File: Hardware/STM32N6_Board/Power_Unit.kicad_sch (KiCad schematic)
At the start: 69 parts, among them J1 Conn_01x02_Pin, J2 Conn_01x02_Pin

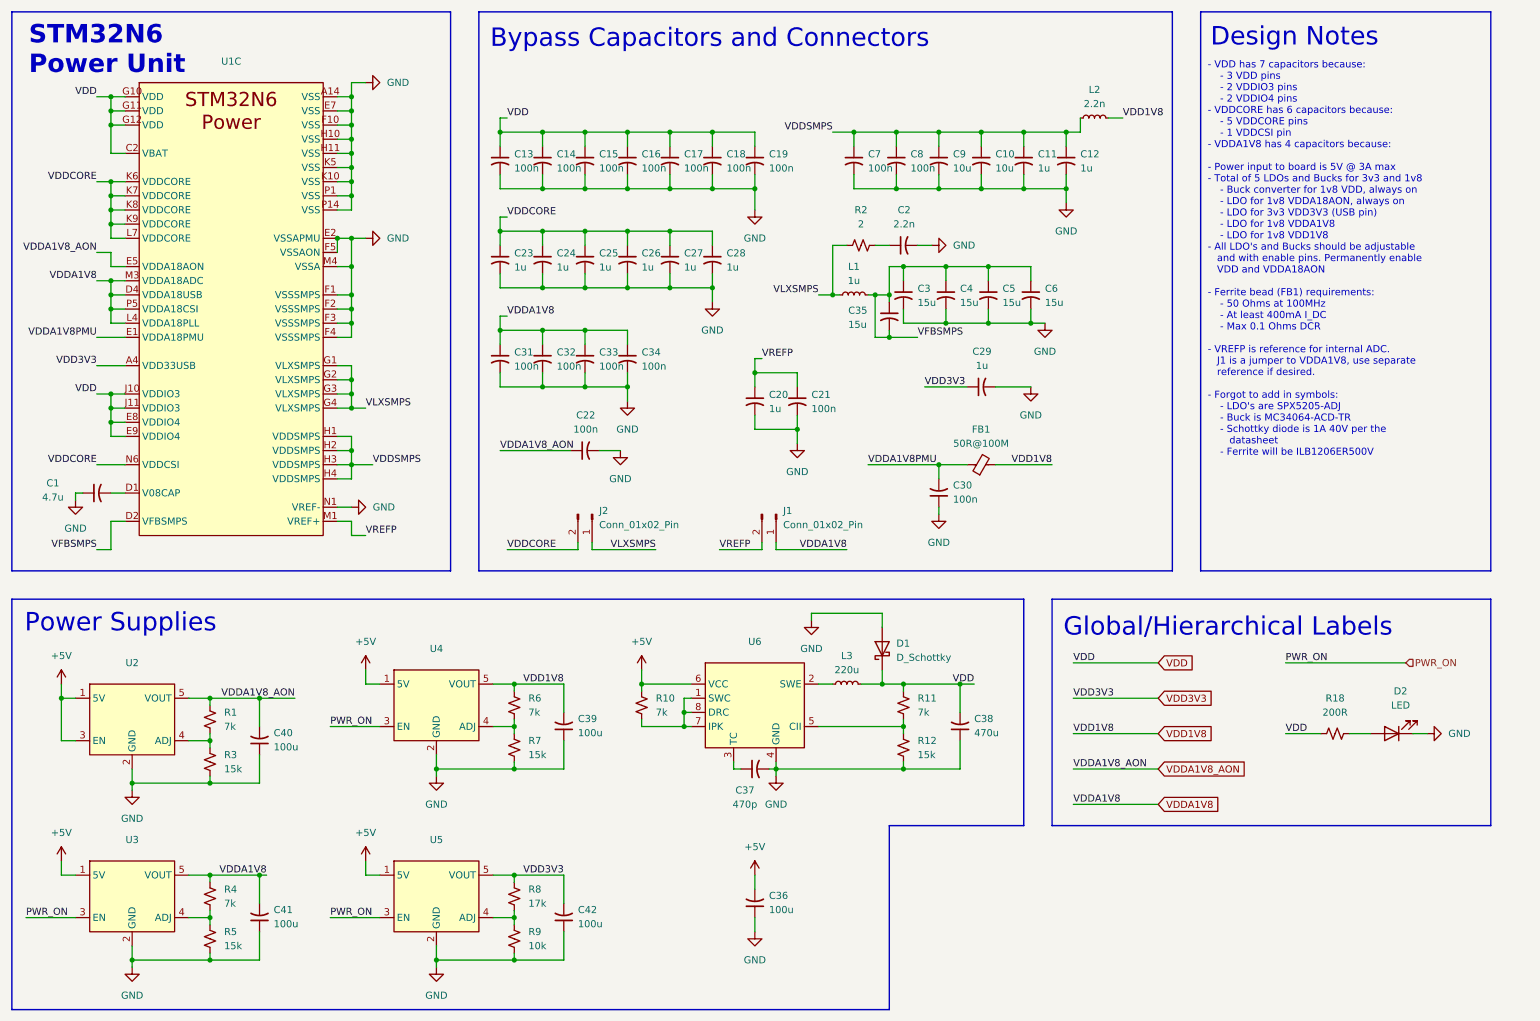
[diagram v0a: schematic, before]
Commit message: Completed wiring of the Analog unit.
- CSI and USB buses are created, yet to be connected with connectors
- Next will be pin selection, and drawing in FMC SDRAM
- Then will be routing GPIOs as buses, and connecting with connectors
- Finally, board layout.
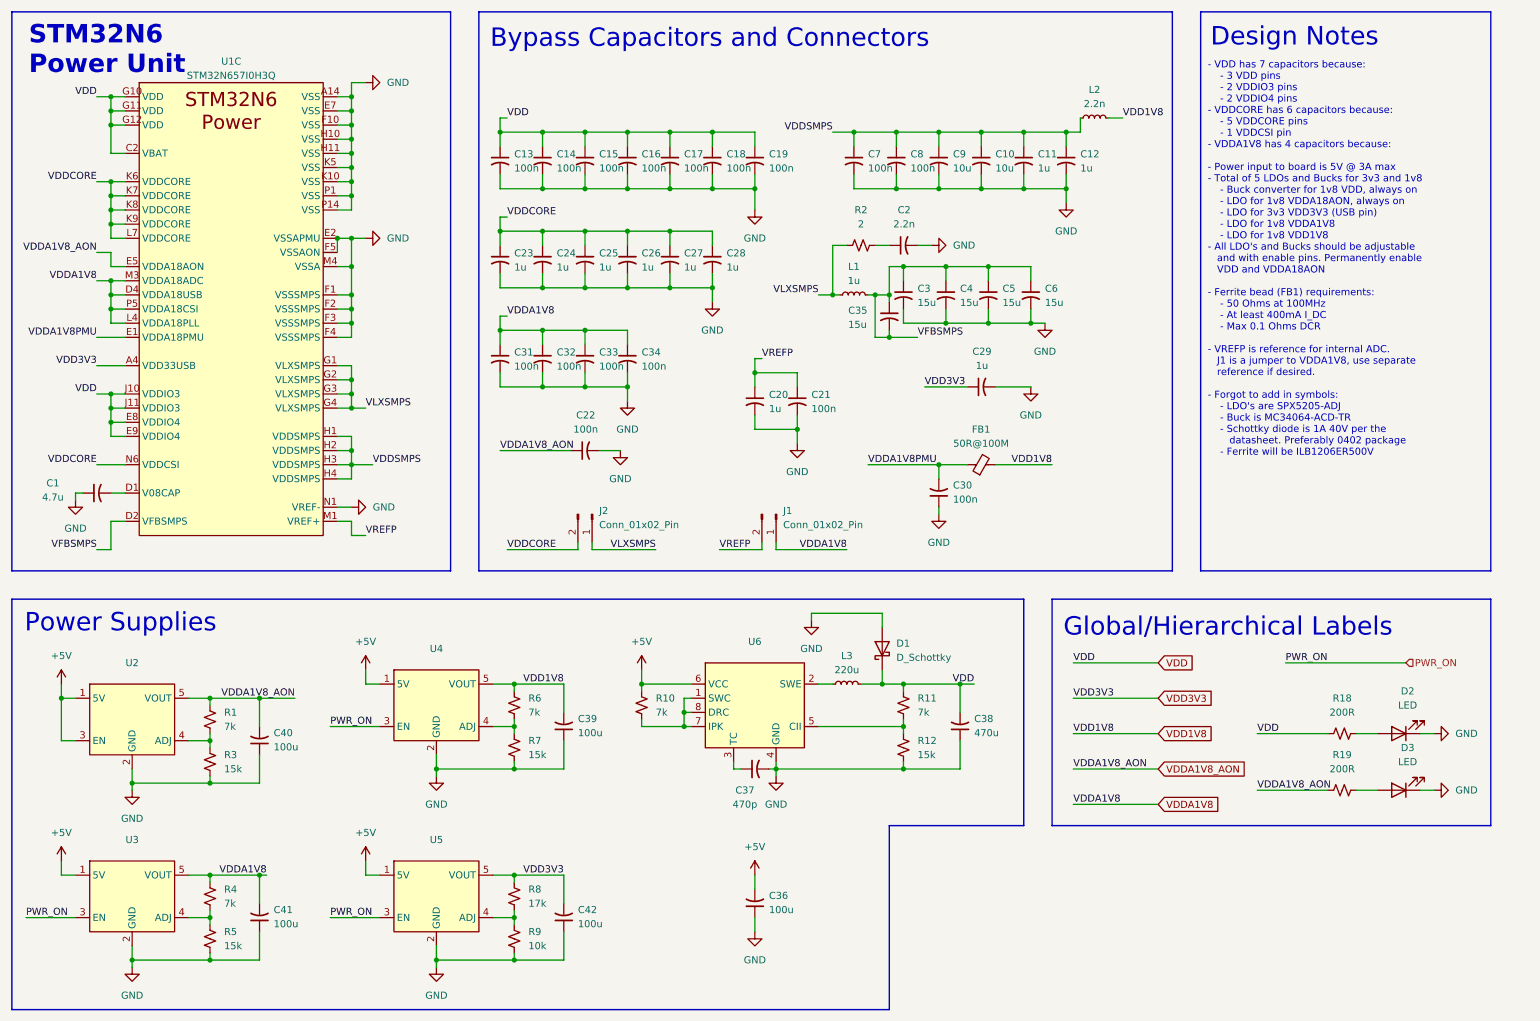
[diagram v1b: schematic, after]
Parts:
- added D3: LED, symbol Device:LED
- added R19: 200R, symbol Device:R_Small_US
- U1: value ~ -> STM32N657I0H3Q
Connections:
- net GND: now also D3.1 (K)
- net VDDA1V8_AON: now also R19.1
- new net: D3.2 (A), R19.2
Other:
- moved on the sheet: D2, R18

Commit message: Completed the schematic.
- The schematic is complete.
- ERC checker, footprint assignment, and PCB board design left
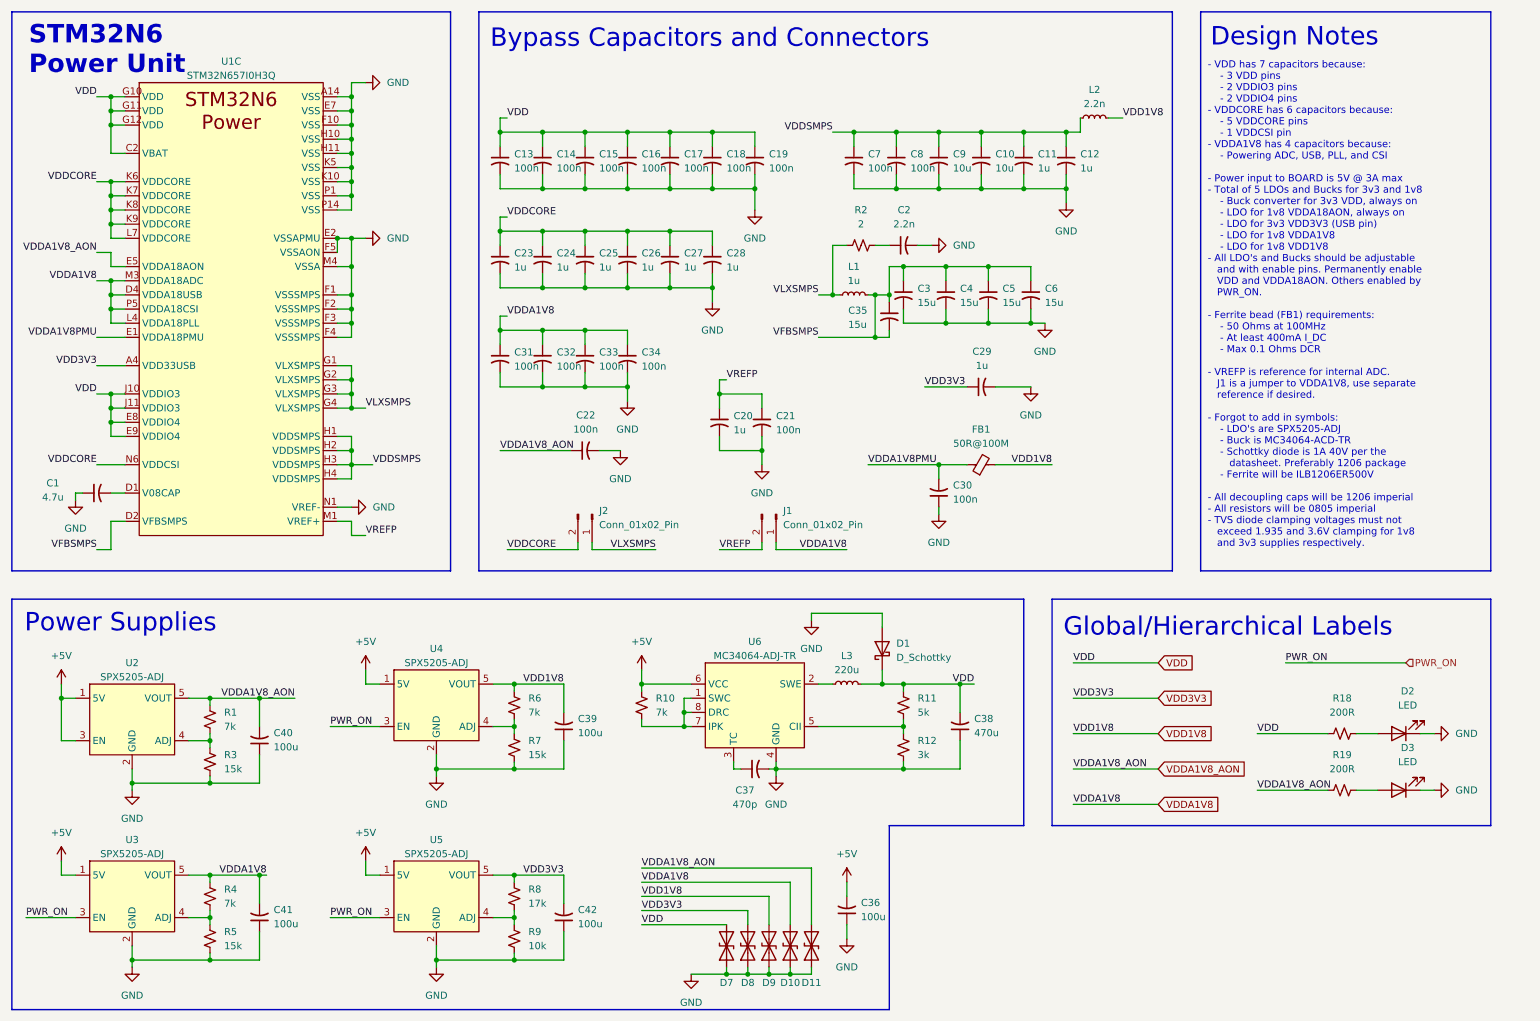
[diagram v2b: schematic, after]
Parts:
- added D10, D11, D7, D8, D9: D_TVS, symbol Device:D_TVS
- R11: value 7k -> 5k
- R12: value 15k -> 3k
- U2, U3, U4, U5: value ~ -> SPX5205-ADJ
- U6: value ~ -> MC34064-ADJ-TR
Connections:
- net GND: now also D10.1 (A1), D11.1 (A1), D7.1 (A1), D8.1 (A1), D9.1 (A1)
- net VDD: now also D7.2 (A2)
- net VDD1V8: now also D9.2 (A2)
- net VDD3V3: now also D8.2 (A2)
- net VDDA1V8: now also D10.2 (A2)
- net VDDA1V8_AON: now also D11.2 (A2)
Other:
- note added: "- VDD has 7 capacitors because: - 3 VDD pins - 2 VDDIO3 pins - 2 VDDIO4 pins - VDDCORE has 6 capacitors because: - 5 VDDCORE pins - 1 VDDCSI pin - VDDA1V8 has 4 capacitors because: - Powering ADC, USB, PLL, and CSI - Power input to BOARD is 5V @ 3A max - Total of 5 LDOs and Bucks for 3v3 and 1v8 - Buck converter for 3v3 VDD, always on - LDO for 1v8 VDDA18AON, always on - LDO for 3v3 VDD3V3 (USB p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"
- note removed: "- VDD has 7 capacitors because: - 3 VDD pins - 2 VDDIO3 pins - 2 VDDIO4 pins - VDDCORE has 6 capacitors because: - 5 VDDCORE pins - 1 VDDCSI pin - VDDA1V8 has 4 capacitors because: - Power input to board is 5V @ 3A max - Total of 5 LDOs and Bucks for 3v3 and 1v8 - Buck converter for 1v8 VDD, always on - LDO for 1v8 VDDA18AON, always on - LDO for 3v3 VDD3V3 (USB pin) - LDO for 1v8 VDDA1V8 - LDO fo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"
- moved on the sheet: C20, C21, C36

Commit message: Made fixes to remove ERC errors
- 1 remaining error, but > 100 warnings D:
- The remaining error is a bug within KiCAD I believe
- Next is footprint assignment
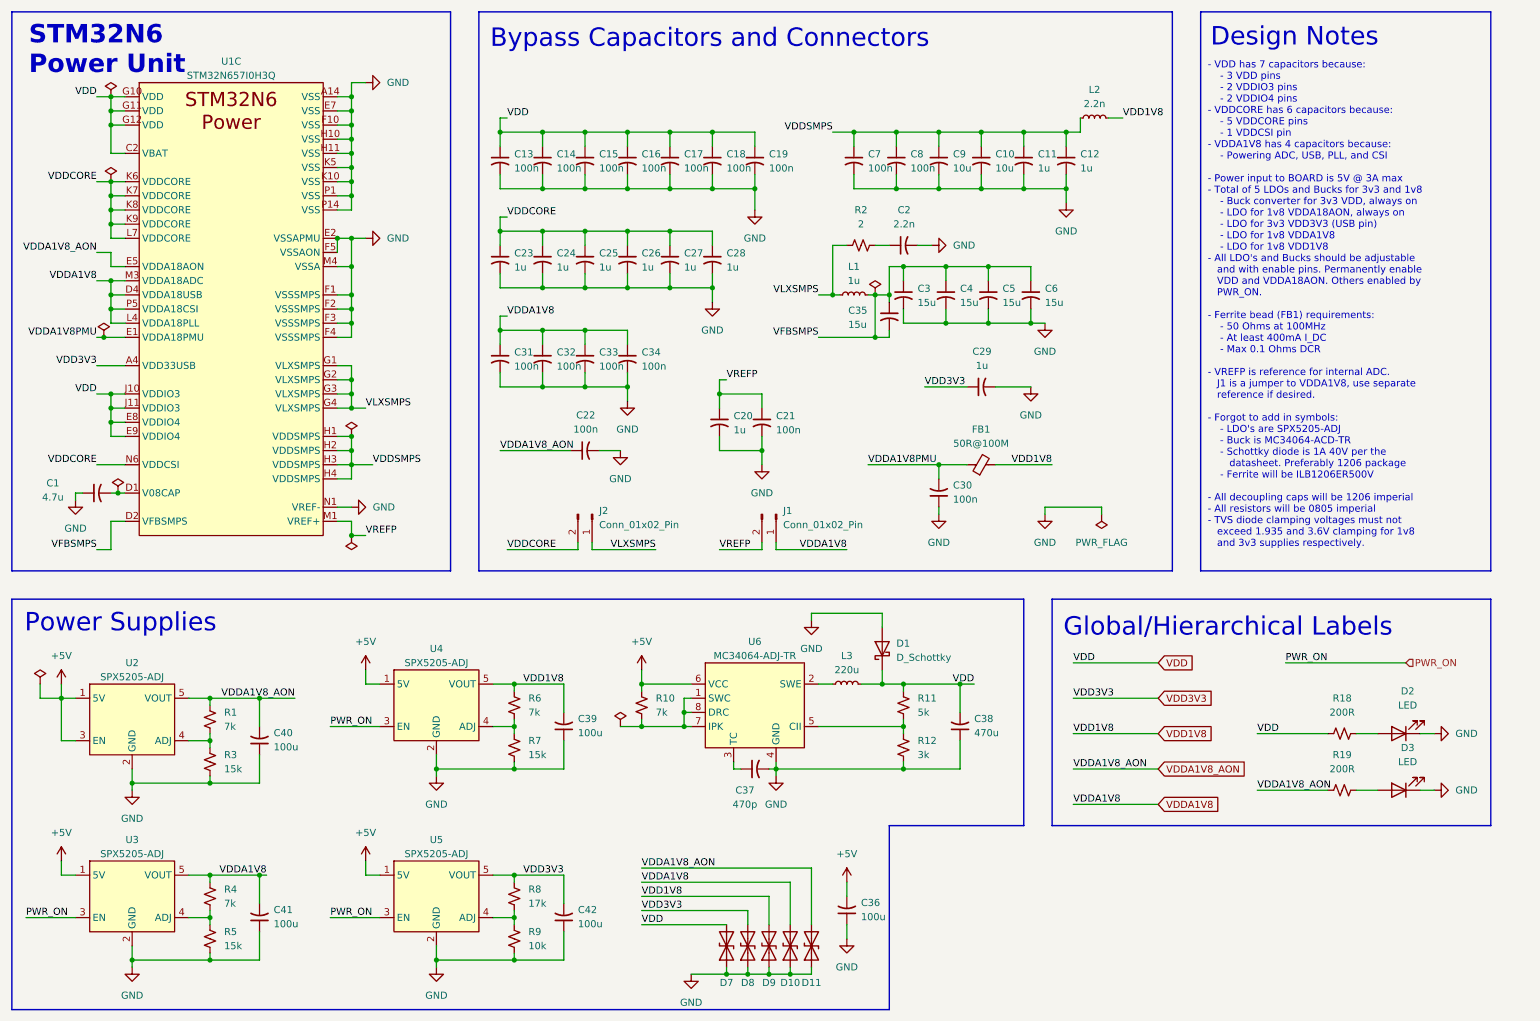
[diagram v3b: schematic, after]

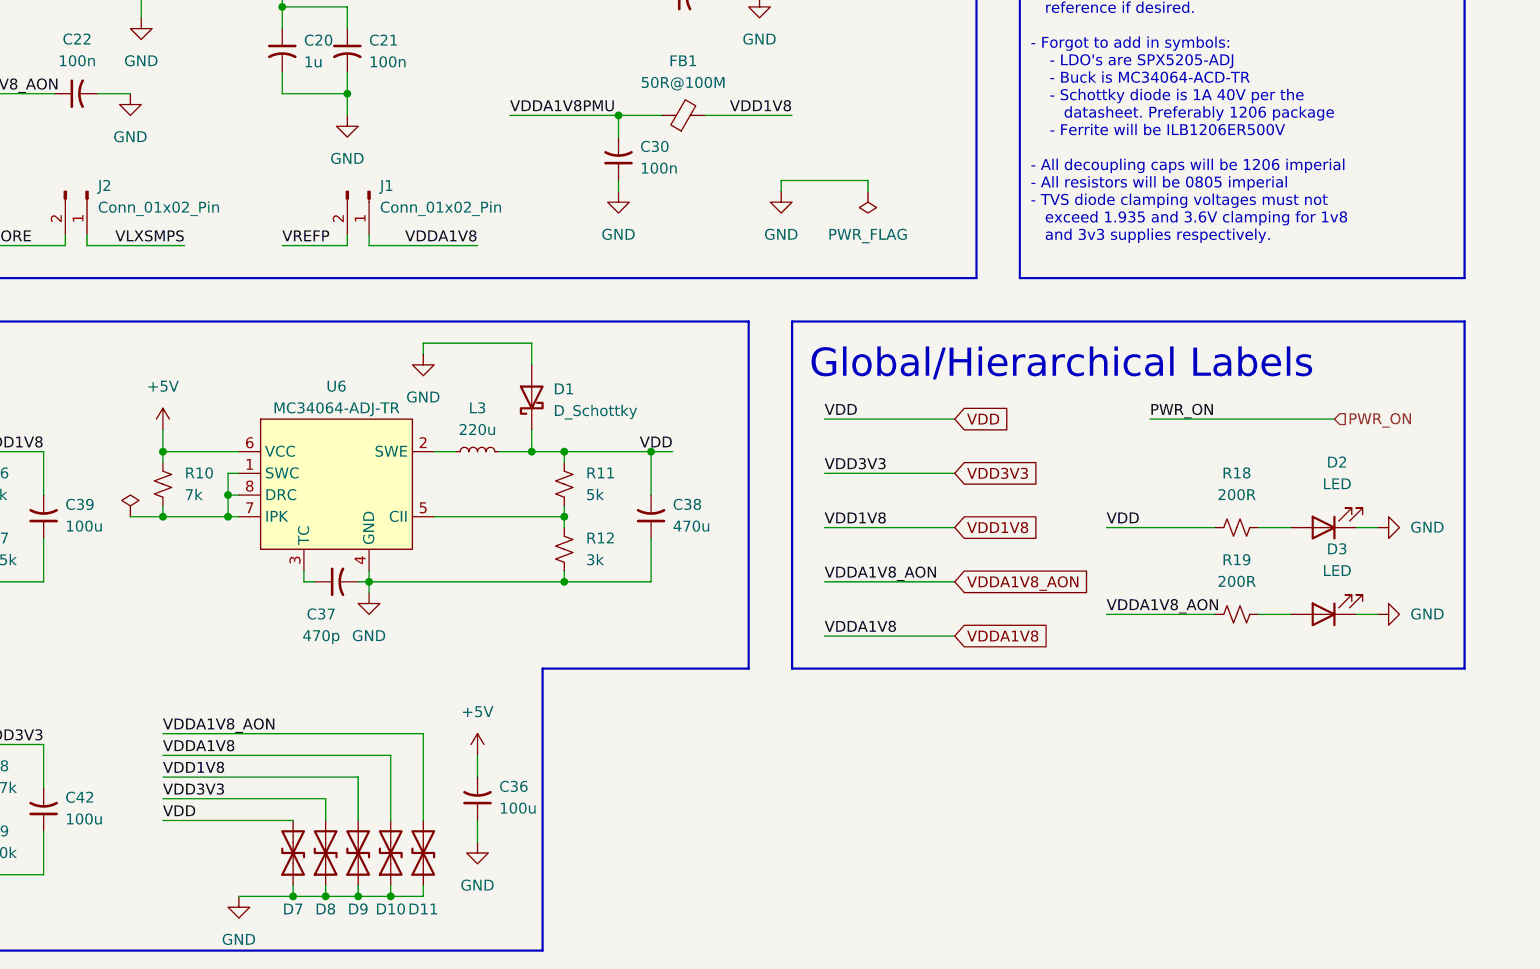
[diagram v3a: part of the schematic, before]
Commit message: Completed schematic layout, ERC check, and footprint assignment
- Completed and checked the schematic layout
- Ran the ERC check; no errors (but lots of (checked) warnings)
- Assigned footprints. Most in std lib, others in footprints.pretty
- Imported the components to the PCB Editor, and fixed errors
- All that's left is PCB layout!
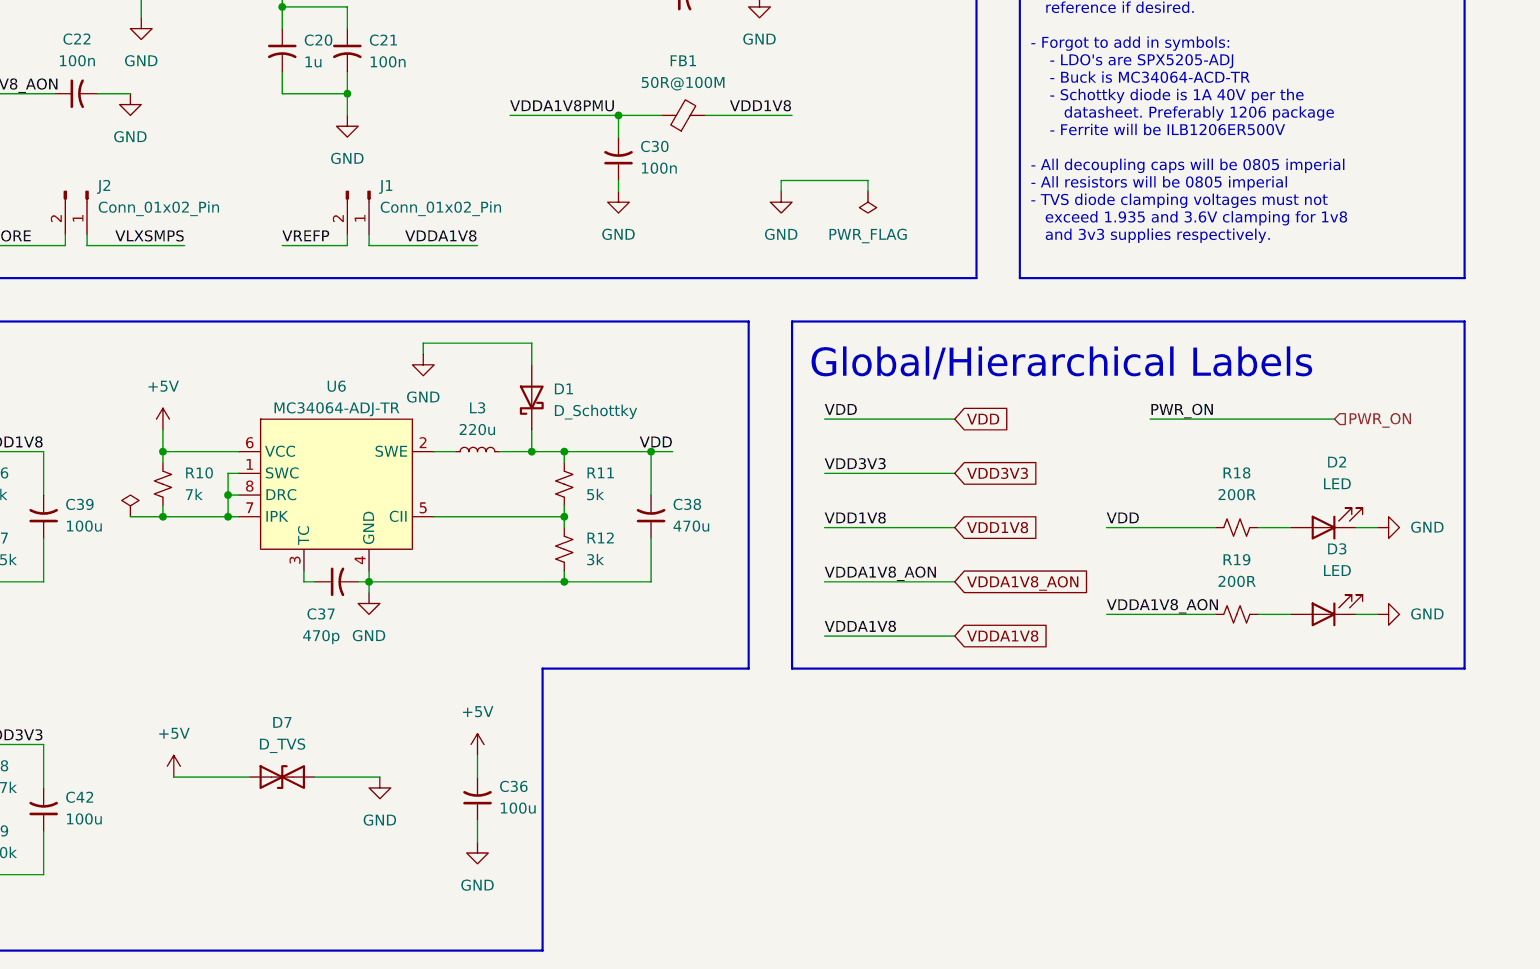
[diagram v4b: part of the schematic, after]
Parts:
- removed D10, D11, D8, D9: D_TVS, symbol Device:D_TVS
- C1, C10, C11, C12, C13, C14, C15, C16, C17, C18, C19, C2, C20, C21, C22, C23, C24, C25, C26, C27, C28, C29, C3, C30, C31, C32, C33, C34, C35, C36, C37, C38, C39, C4, C40, C41, C42, C5, C6, C7, C8, C9: footprint (none) -> Capacitor_SMD:C_0805_2012Metric_Pad1.18x1.45mm_HandSolder
- D1: footprint (none) -> STM32N6_Footprints:Schottky_DIOM4325X250N
- D2, D3: footprint (none) -> LED_SMD:LED_0603_1608Metric_Pad1.05x0.95mm_HandSolder
- D7: footprint (none) -> LED_SMD:LED_0805_2012Metric_Pad1.15x1.40mm_HandSolder
- FB1, L1, L2, L3: footprint (none) -> Inductor_SMD:L_1206_3216Metric_Pad1.42x1.75mm_HandSolder
- J1, J2: footprint (none) -> Connector_PinHeader_2.54mm:PinHeader_1x02_P2.54mm_Vertical
- R1, R10, R11, R12, R18, R19, R2, R3, R4, R5, R6, R7, R8, R9: footprint (none) -> Resistor_SMD:R_0805_2012Metric_Pad1.20x1.40mm_HandSolder
- U1: footprint (none) -> STM32N6_Footprints:STM32N657I0H3Q_VFBGA178_14x14
- U2, U3, U4, U5: footprint (none) -> Package_TO_SOT_SMD:SOT-23-5
- U6: footprint (none) -> Package_SO:SO-8_3.9x4.9mm_P1.27mm
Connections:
- net +5V: now also D7.1 (A1)
- net GND: now also D7.2 (A2); no longer D7.1 (A1)
- net VDD: no longer D7.2 (A2)
